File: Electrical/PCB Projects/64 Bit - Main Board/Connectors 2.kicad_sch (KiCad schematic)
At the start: 32 parts, among them J10 M20-7920242R, J11 M20-7920242R, J12 M20-7920242R, J13 M20-7920242R, J17 M20-7920242R, J18 M20-7920242R, J6 M20-7920242R, J8 M20-7920242R, J9 M20-7920242R, Q11 2N7002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

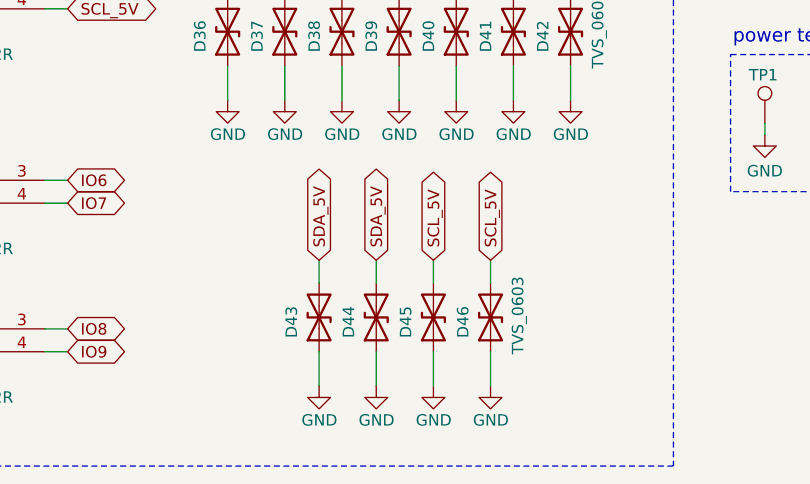
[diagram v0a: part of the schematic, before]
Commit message: finished routing - added photoresistor to analog pin. Updated STM32Cube setup. Final stages of hardware design
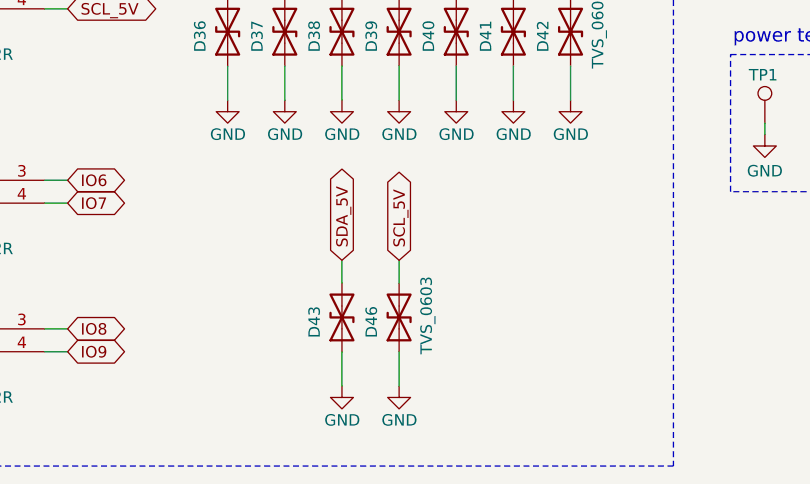
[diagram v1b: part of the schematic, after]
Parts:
- removed D44, D45: TVS_0603, Resistor_SMD:R_0603_1608Metric, symbol HDD_CLK_V6.0:CG0603MLC-05LE
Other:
- moved on the sheet: D43, D46

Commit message: slight changes
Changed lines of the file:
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@@
 	(text "5V I2C breakout"
 		(exclude_from_sim no)
-		(at 57.912 140.716 90)
+		(at 56.642 140.716 90)
 		(effects
 			(font
@@
 	)
 	(junction
-		(at 59.69 121.92)
+		(at 58.42 121.92)
 		(diameter 0)
 		(color 0 0 0 0)
@@
 	(wire
 		(pts
-			(xy 59.69 121.92) (xy 64.77 121.92)
+			(xy 58.42 121.92) (xy 64.77 121.92)
 		)
 		(stroke
@@
 	(wire
 		(pts
-			(xy 59.69 138.43) (xy 59.69 121.92)
+			(xy 58.42 138.43) (xy 58.42 121.92)
 		)
 		(stroke
@@
 	(wire
 		(pts
-			(xy 59.69 121.92) (xy 59.69 118.11)
+			(xy 58.42 121.92) (xy 58.42 118.11)
 		)
 		(stroke
@@
 	(wire
 		(pts
-			(xy 64.77 138.43) (xy 59.69 138.43)
+			(xy 64.77 138.43) (xy 58.42 138.43)
 		)
 		(stroke
@@
 	(symbol
 		(lib_id "power:+5V")
-		(at 59.69 118.11 0)
+		(at 58.42 118.11 0)
 		(unit 1)
 		(exclude_from_sim no)
@@
 		(dnp no)
 		(property "Reference" "#PWR0151"
-			(at 59.69 121.92 0)
+			(at 58.42 121.92 0)
 			(effects
 				(font
@@
 		)
 		(property "Value" "+5V"
-			(at 59.69 114.046 0)
+			(at 58.42 114.046 0)
 			(effects
 				(font
@@
 		)
 		(property "Footprint" ""
-			(at 59.69 118.11 0)
+			(at 58.42 118.11 0)
 			(effects
 				(font
@@
 		)
 		(property "Datasheet" ""
-			(at 59.69 118.11 0)
+			(at 58.42 118.11 0)
 			(effects
 				(font
@@
 		)
 		(property "Description" ""
-			(at 59.69 118.11 0)
+			(at 58.42 118.11 0)
 			(effects
 				(font
